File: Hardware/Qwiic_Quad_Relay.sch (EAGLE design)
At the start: 69 parts, among them J2 Qwiic Right Angle, J3 Qwiic Right Angle, J4 POWER_JACK, J9 AVR_SPI_PROG_3X2TESTPOINTS, K1 RELAY-SPDT-JZC-11F, K2 RELAY-SPDT-JZC-11F, K3 RELAY-SPDT-JZC-11F, K4 RELAY-SPDT-JZC-11F, Q1 600mA/40V, Q2 600mA/40V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

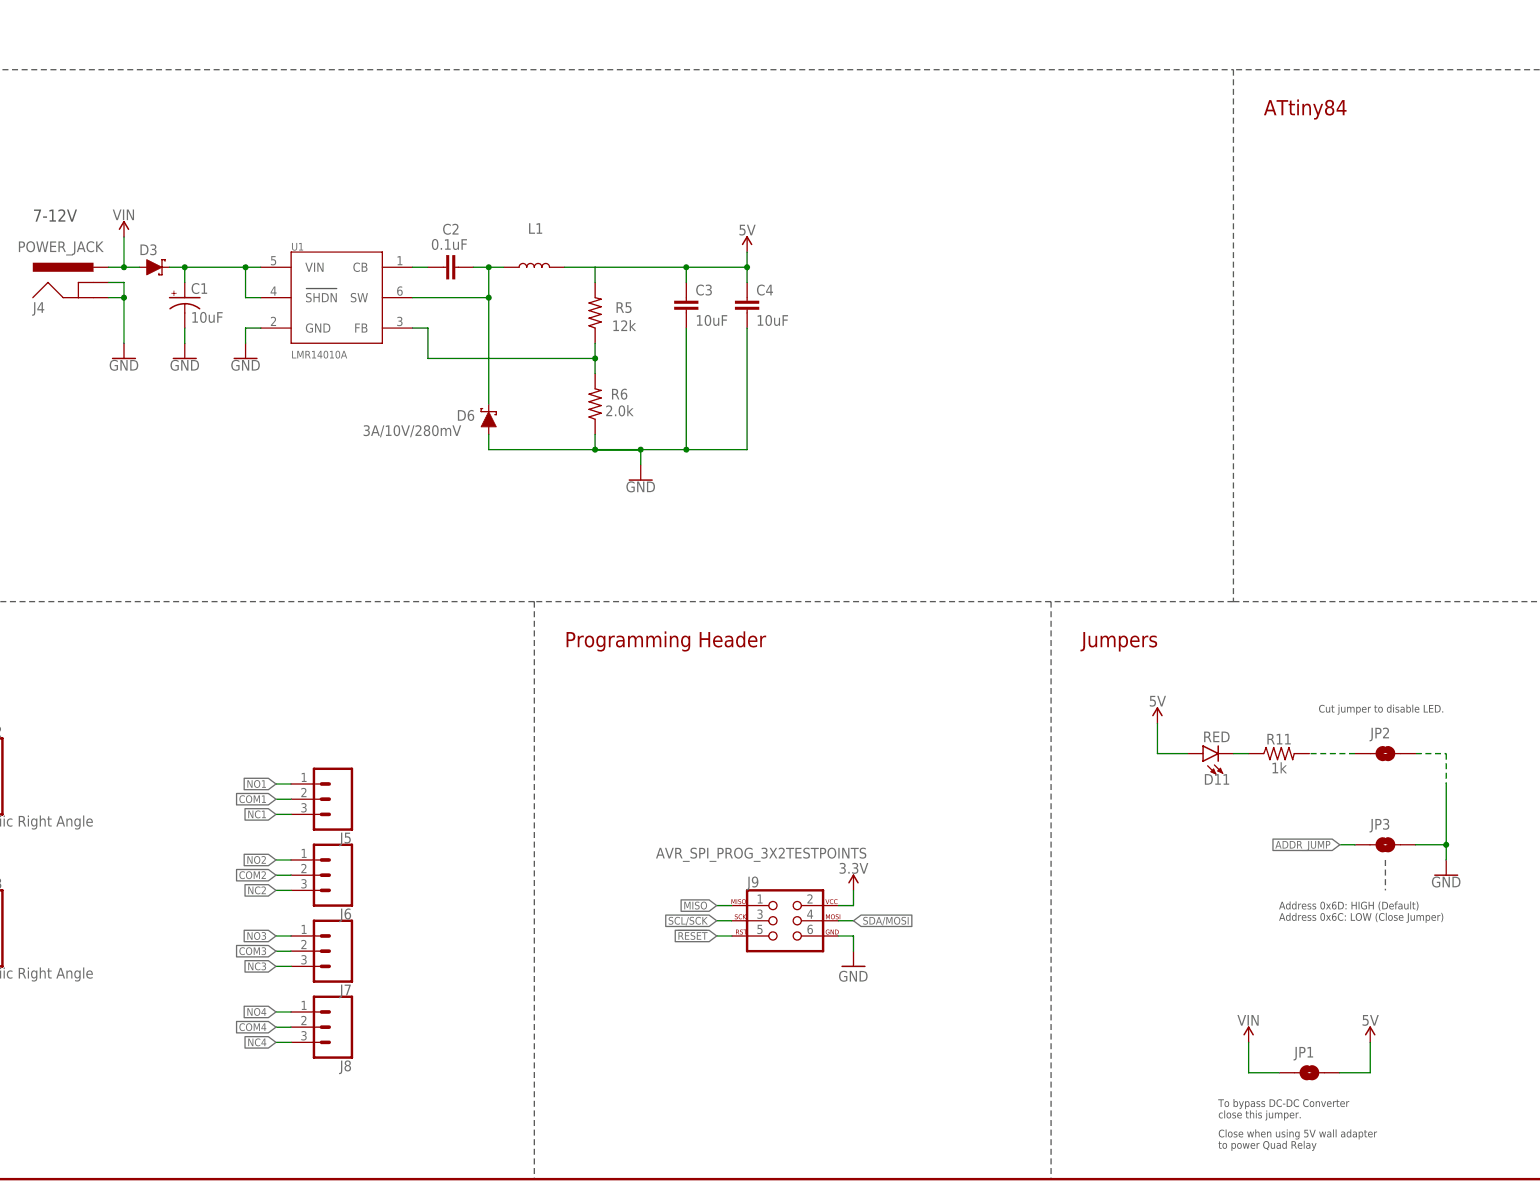
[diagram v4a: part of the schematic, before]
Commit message: Fixes bypass
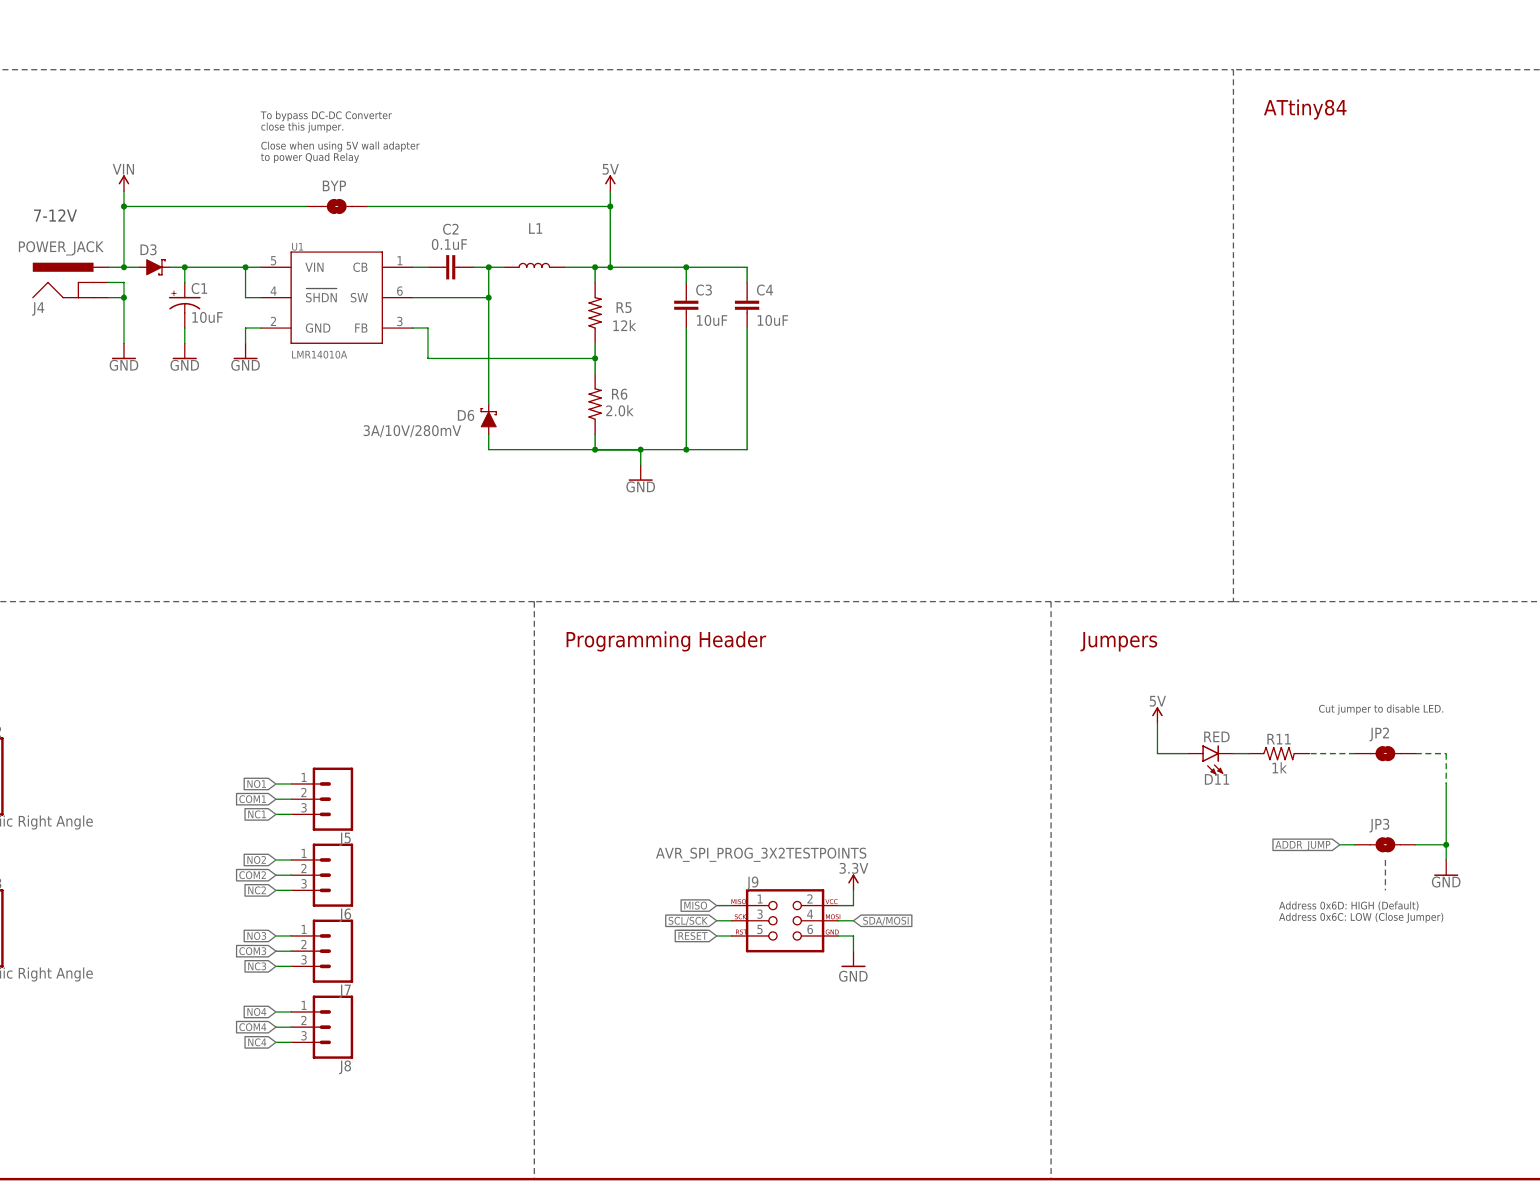
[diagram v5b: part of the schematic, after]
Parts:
- removed JP1: JUMPER-SMT_2_NO_SILK, SparkFun-Jumpers:JUMPER-SMT_2_NO_SILK
- added BYP: JUMPER-SMT_2_NO_SILK, SparkFun-Jumpers:JUMPER-SMT_2_NO_SILK
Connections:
- net 5V: now also BYP.2; no longer JP1.2
- net VIN: now also BYP.1; no longer JP1.1
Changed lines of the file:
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@@
 <part name="D6" library="SparkFun-DiscreteSemi" deviceset="DIODE-SCHOTTKY" device="-BAT60A" value="3A/10V/280mV"/>
 <part name="JP2" library="SparkFun-Jumpers" deviceset="JUMPER-SMT_2_NO" device="_SILK" package3d_urn="urn:adsk.eagle:package:39279/1"/>
-<part name="JP1" library="SparkFun-Jumpers" deviceset="JUMPER-SMT_2_NO" device="_SILK" package3d_urn="urn:adsk.eagle:package:39279/1"/>
-<part name="SUPPLY18" library="SparkFun-PowerSymbols" deviceset="VIN" device=""/>
-<part name="SUPPLY20" library="SparkFun-PowerSymbols" deviceset="5V" device=""/>
+<part name="BYP" library="SparkFun-Jumpers" deviceset="JUMPER-SMT_2_NO" device="_SILK" package3d_urn="urn:adsk.eagle:package:39279/1"/>
 <part name="GND7" library="SparkFun-PowerSymbols" deviceset="GND" device=""/>
 </parts>
@@
 <text x="540.004" y="77.978" size="1.27" layer="97" font="vector">Cut jumper to disable LED.</text>
 <text x="500.38" y="88.9" size="2.54" layer="94" font="vector">Jumpers</text>
-<text x="523.24" y="10.16" size="1.27" layer="97" font="vector">To bypass DC-DC Converter
+<text x="363.22" y="175.26" size="1.27" layer="97" font="vector">To bypass DC-DC Converter
 close this jumper. </text>
-<text x="523.24" y="5.08" size="1.27" layer="97" font="vector">Close when using 5V wall adapter
+<text x="363.22" y="170.18" size="1.27" layer="97" font="vector">Close when using 5V wall adapter
 to power Quad Relay</text>
 </plain>
@@
 <attribute name="VALUE" x="340.36" y="136.906" size="1.778" layer="96" align="top-center"/>
 </instance>
-<instance part="SUPPLY16" gate="G$1" x="444.5" y="154.94" smashed="yes">
-<attribute name="VALUE" x="444.5" y="157.734" size="1.778" layer="96" align="bottom-center"/>
+<instance part="SUPPLY16" gate="G$1" x="421.64" y="165.1" smashed="yes">
+<attribute name="VALUE" x="421.64" y="167.894" size="1.778" layer="96" align="bottom-center"/>
 </instance>
 <instance part="SUPPLY17" gate="G$1" x="462.28" y="48.26" smashed="yes">
@@
 <attribute name="NAME" x="342.9" y="154.432" size="1.778" layer="95" font="vector"/>
 </instance>
-<instance part="SUPPLY19" gate="G$1" x="340.36" y="157.48" smashed="yes">
-<attribute name="VALUE" x="340.36" y="160.274" size="1.778" layer="96" align="bottom-center"/>
+<instance part="SUPPLY19" gate="G$1" x="340.36" y="165.1" smashed="yes">
+<attribute name="VALUE" x="340.36" y="167.894" size="1.778" layer="96" align="bottom-center"/>
 </instance>
 <instance part="GND18" gate="1" x="561.34" y="50.8" smashed="yes">
@@
 <attribute name="NAME" x="548.64" y="73.66" size="1.778" layer="95" font="vector"/>
 </instance>
-<instance part="JP1" gate="G$1" x="538.48" y="17.78" smashed="yes">
-<attribute name="NAME" x="535.94" y="20.32" size="1.778" layer="95" font="vector"/>
-</instance>
-<instance part="SUPPLY18" gate="G$1" x="528.32" y="22.86" smashed="yes">
-<attribute name="VALUE" x="528.32" y="25.654" size="1.778" layer="96" align="bottom-center"/>
-</instance>
-<instance part="SUPPLY20" gate="G$1" x="548.64" y="22.86" smashed="yes">
-<attribute name="VALUE" x="548.64" y="25.654" size="1.778" layer="96" align="bottom-center"/>
+<instance part="BYP" gate="G$1" x="375.92" y="162.56" smashed="yes">
+<attribute name="NAME" x="373.38" y="165.1" size="1.778" layer="95" font="vector"/>
 </instance>
 <instance part="GND7" gate="1" x="462.28" y="35.56" smashed="yes">
@@
 </segment>
 <segment>
+<pinref part="R1" gate="G$1" pin="2"/>
+<pinref part="SUPPLY13" gate="G$1" pin="5V"/>
+<wire x1="314.96" y1="251.46" x2="314.96" y2="254" width="0.1524" layer="91"/>
+</segment>
+<segment>
+<pinref part="SUPPLY3" gate="G$1" pin="5V"/>
+<pinref part="R3" gate="G$1" pin="2"/>
+<wire x1="375.92" y1="254" x2="375.92" y2="248.92" width="0.1524" layer="91"/>
+</segment>
+<segment>
+<pinref part="R7" gate="G$1" pin="2"/>
+<pinref part="SUPPLY8" gate="G$1" pin="5V"/>
+<wire x1="439.42" y1="248.92" x2="439.42" y2="254" width="0.1524" layer="91"/>
+</segment>
+<segment>
+<pinref part="R9" gate="G$1" pin="2"/>
+<pinref part="SUPPLY10" gate="G$1" pin="5V"/>
+<wire x1="500.38" y1="248.92" x2="500.38" y2="254" width="0.1524" layer="91"/>
+</segment>
+<segment>
+<pinref part="BYP" gate="G$1" pin="2"/>
 <pinref part="L1" gate="G$1" pin="2"/>
-<pinref part="R5" gate="G$1" pin="2"/>
-<wire x1="419.1" y1="149.86" x2="419.1" y2="152.4" width="0.1524" layer="91"/>
-<wire x1="419.1" y1="152.4" x2="414.02" y2="152.4" width="0.1524" layer="91"/>
 <pinref part="C3" gate="G$1" pin="1"/>
-<wire x1="419.1" y1="152.4" x2="434.34" y2="152.4" width="0.1524" layer="91"/>
+<wire x1="414.02" y1="152.4" x2="419.1" y2="152.4" width="0.1524" layer="91"/>
+<wire x1="419.1" y1="152.4" x2="421.64" y2="152.4" width="0.1524" layer="91"/>
+<wire x1="421.64" y1="152.4" x2="434.34" y2="152.4" width="0.1524" layer="91"/>
 <wire x1="434.34" y1="152.4" x2="434.34" y2="149.86" width="0.1524" layer="91"/>
 <wire x1="434.34" y1="152.4" x2="444.5" y2="152.4" width="0.1524" layer="91"/>
@@
 <wire x1="444.5" y1="152.4" x2="444.5" y2="149.86" width="0.1524" layer="91"/>
 <pinref part="SUPPLY16" gate="G$1" pin="5V"/>
-<wire x1="444.5" y1="152.4" x2="444.5" y2="154.94" width="0.1524" layer="91"/>
-<junction x="444.5" y="152.4"/>
-</segment>
-<segment>
-<pinref part="R1" gate="G$1" pin="2"/>
-<pinref part="SUPPLY13" gate="G$1" pin="5V"/>
-<wire x1="314.96" y1="251.46" x2="314.96" y2="254" width="0.1524" layer="91"/>
-</segment>
-<segment>
-<pinref part="SUPPLY3" gate="G$1" pin="5V"/>
-<pinref part="R3" gate="G$1" pin="2"/>
-<wire x1="375.92" y1="254" x2="375.92" y2="248.92" width="0.1524" layer="91"/>
-</segment>
-<segment>
-<pinref part="R7" gate="G$1" pin="2"/>
-<pinref part="SUPPLY8" gate="G$1" pin="5V"/>
-<wire x1="439.42" y1="248.92" x2="439.42" y2="254" width="0.1524" layer="91"/>
-</segment>
-<segment>
-<pinref part="R9" gate="G$1" pin="2"/>
-<pinref part="SUPPLY10" gate="G$1" pin="5V"/>
-<wire x1="500.38" y1="248.92" x2="500.38" y2="254" width="0.1524" layer="91"/>
-</segment>
-<segment>
-<pinref part="JP1" gate="G$1" pin="2"/>
-<wire x1="543.56" y1="17.78" x2="548.64" y2="17.78" width="0.1524" layer="91"/>
-<pinref part="SUPPLY20" gate="G$1" pin="5V"/>
-<wire x1="548.64" y1="17.78" x2="548.64" y2="22.86" width="0.1524" layer="91"/>
+<pinref part="R5" gate="G$1" pin="2"/>
+<wire x1="419.1" y1="152.4" x2="419.1" y2="149.86" width="0.1524" layer="91"/>
+<junction x="419.1" y="152.4"/>
+<wire x1="421.64" y1="152.4" x2="421.64" y2="162.56" width="0.1524" layer="91"/>
+<junction x="421.64" y="152.4"/>
+<wire x1="421.64" y1="162.56" x2="421.64" y2="165.1" width="0.1524" layer="91"/>
+<wire x1="381" y1="162.56" x2="421.64" y2="162.56" width="0.1524" layer="91"/>
+<junction x="421.64" y="162.56"/>
 </segment>
 </net>
@@
 <wire x1="340.36" y1="152.4" x2="342.9" y2="152.4" width="0.1524" layer="91"/>
 <pinref part="SUPPLY19" gate="G$1" pin="VIN"/>
-<wire x1="340.36" y1="152.4" x2="340.36" y2="157.48" width="0.1524" layer="91"/>
+<wire x1="340.36" y1="152.4" x2="340.36" y2="162.56" width="0.1524" layer="91"/>
 <junction x="340.36" y="152.4"/>
-</segment>
-<segment>
-<pinref part="JP1" gate="G$1" pin="1"/>
-<wire x1="533.4" y1="17.78" x2="528.32" y2="17.78" width="0.1524" layer="91"/>
-<pinref part="SUPPLY18" gate="G$1" pin="VIN"/>
-<wire x1="528.32" y1="17.78" x2="528.32" y2="22.86" width="0.1524" layer="91"/>
-</segment>
-</net>
+<pinref part="BYP" gate="G$1" pin="1"/>
+<wire x1="340.36" y1="162.56" x2="340.36" y2="165.1" width="0.1524" layer="91"/>
+<wire x1="340.36" y1="162.56" x2="370.84" y2="162.56" width="0.1524" layer="91"/>
+<junction x="340.36" y="162.56"/>
+</segment>
+</net>
